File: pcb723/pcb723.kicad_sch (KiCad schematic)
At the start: 58 parts, among them J1 Conn_01x02_Pin, J2 Conn_01x02_Pin, J3 Conn_02x07_Odd_Even, J4 Conn_02x04_Odd_Even, J5 USB_C_Receptacle_USB2.0_16P, J6 Conn_02x13_Odd_Even, SW1 SW_Push, U1 STM32H723ZGT6, U2 AMS1117-3.3, Y1 8MHz 20pF

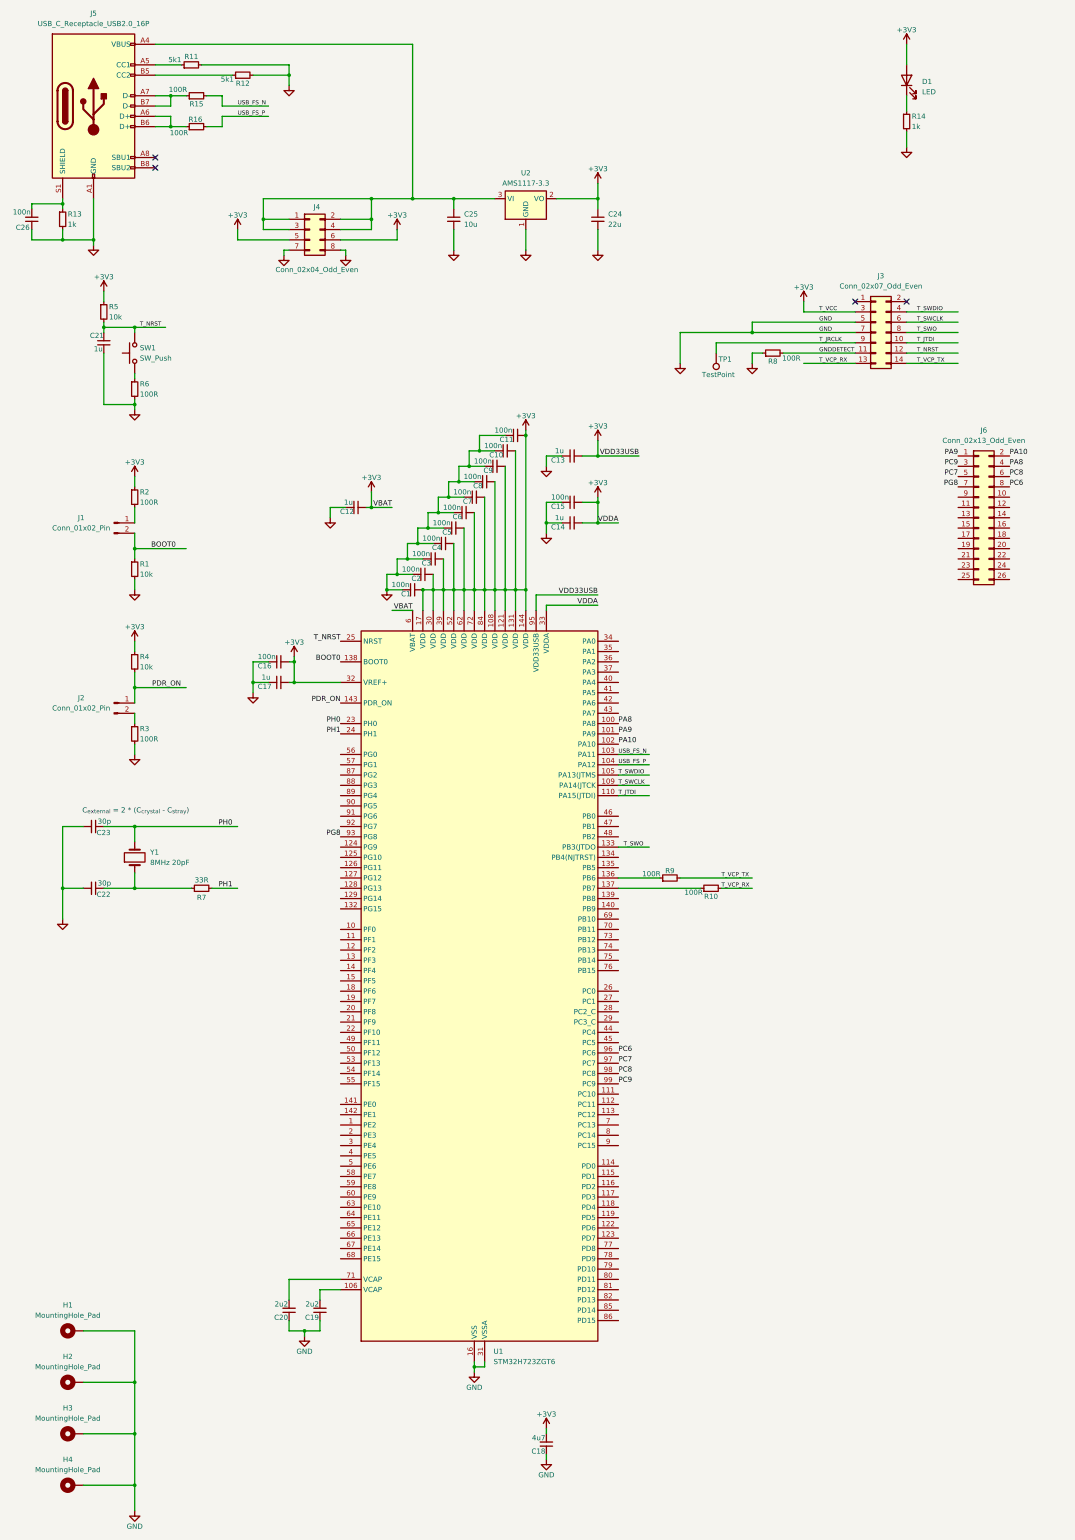
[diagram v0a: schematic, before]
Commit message: Connect starting breakout pins
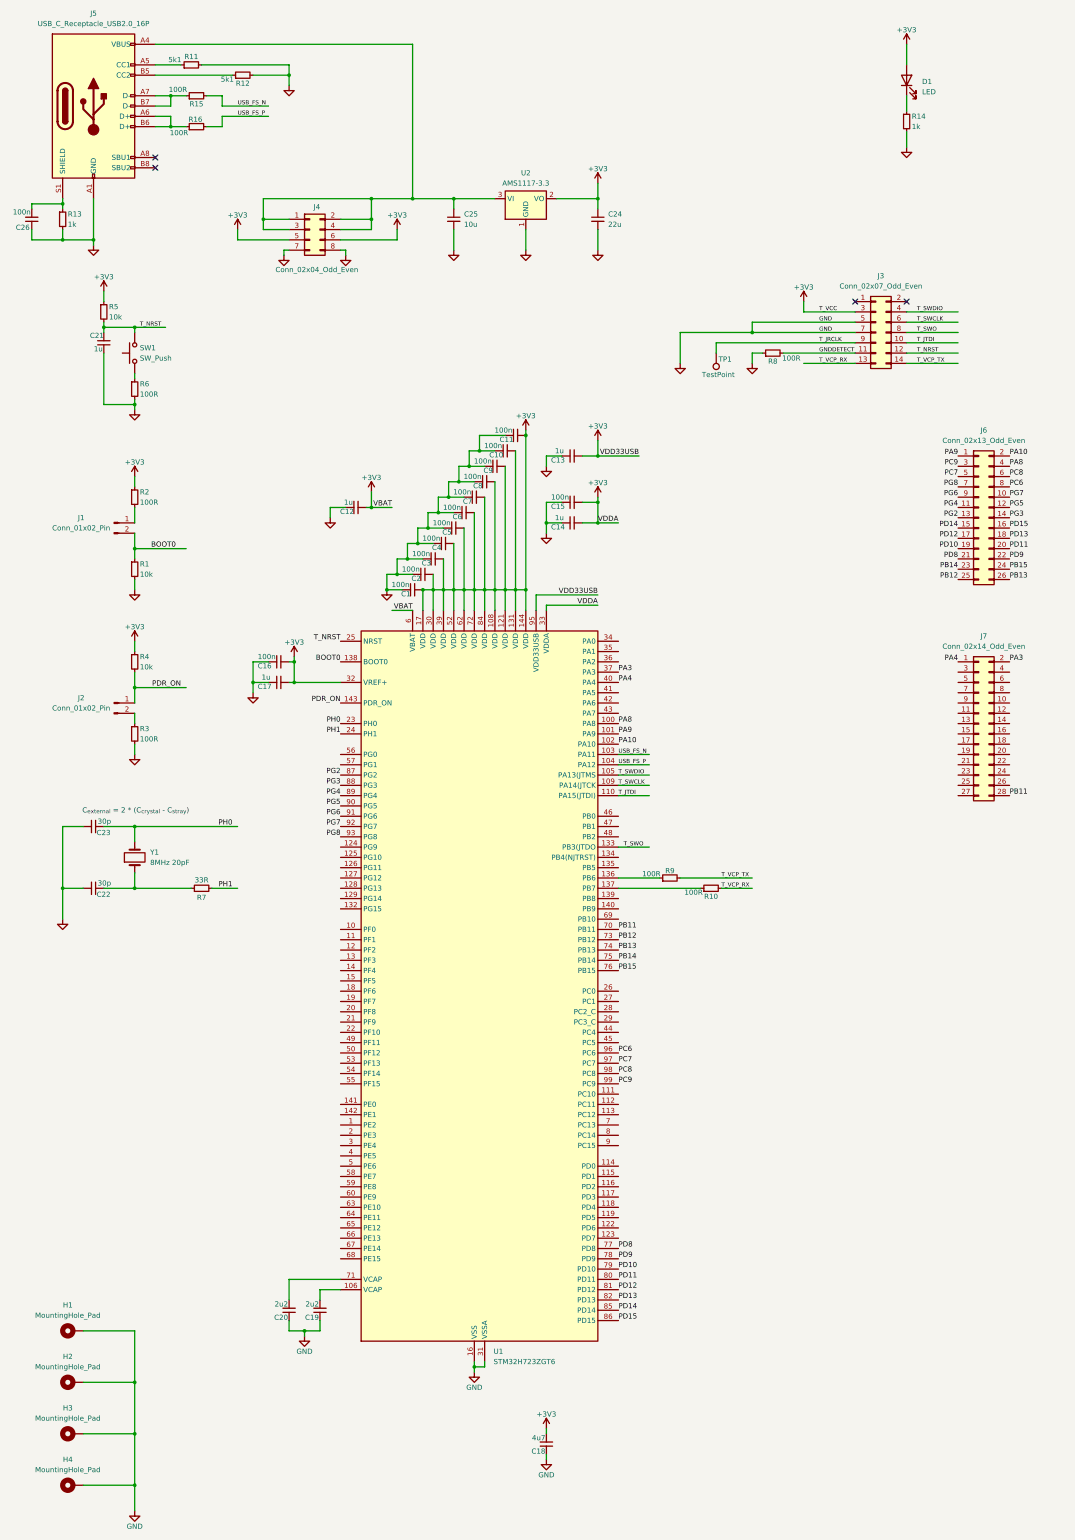
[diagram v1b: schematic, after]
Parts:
- added J7: Conn_02x14_Odd_Even, Connector_PinSocket_2.54mm:PinSocket_2x14_P2.54mm_Vertical, symbol Connector_Generic:Conn_02x14_Odd_Even
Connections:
- net PG7: now reaches J6.10 (Pin_10)
- net PG7: now also U1.92 (PG7)
- net PG4: now reaches J6.11 (Pin_11)
- net PG4: now also U1.89 (PG4)
- net PG5: now reaches J6.12 (Pin_12)
- net PG5: now also U1.90 (PG5)
- net PG2: now reaches J6.13 (Pin_13)
- net PG2: now also U1.87 (PG2)
- net PG3: now reaches J6.14 (Pin_14)
- net PG3: now also U1.88 (PG3)
- net PD14: now reaches J6.15 (Pin_15)
- net PD14: now also U1.85 (PD14)
- net PD15: now reaches J6.16 (Pin_16)
- net PD15: now also U1.86 (PD15)
- net PD12: now reaches J6.17 (Pin_17)
- net PD12: now also U1.81 (PD12)
- net PD13: now reaches J6.18 (Pin_18)
- net PD13: now also U1.82 (PD13)
- net PD10: now reaches J6.19 (Pin_19)
- net PD10: now also U1.79 (PD10)
- net PD11: now reaches J6.20 (Pin_20)
- net PD11: now also U1.80 (PD11)
- net PD8: now reaches J6.21 (Pin_21)
- net PD8: now also U1.77 (PD8)
- net PD9: now reaches J6.22 (Pin_22)
- net PD9: now also U1.78 (PD9)
- net PB14: now reaches J6.23 (Pin_23)
- net PB14: now also U1.75 (PB14)
- net PB15: now reaches J6.24 (Pin_24)
- net PB15: now also U1.76 (PB15)
- net PB12: now reaches J6.25 (Pin_25)
- net PB12: now also U1.73 (PB12)
- net PB13: now reaches J6.26 (Pin_26)
- net PB13: now also U1.74 (PB13)
- net PG6: now reaches J6.9 (Pin_9)
- net PG6: now also U1.91 (PG6)
- net PA3: now reaches U1.37 (PA3)
- net PA3: now also J7.2 (Pin_2)
- net PA4: now reaches U1.40 (PA4)
- net PA4: now also J7.1 (Pin_1)
- net PB11: now reaches U1.70 (PB11)
- net PB11: now also J7.28 (Pin_28)

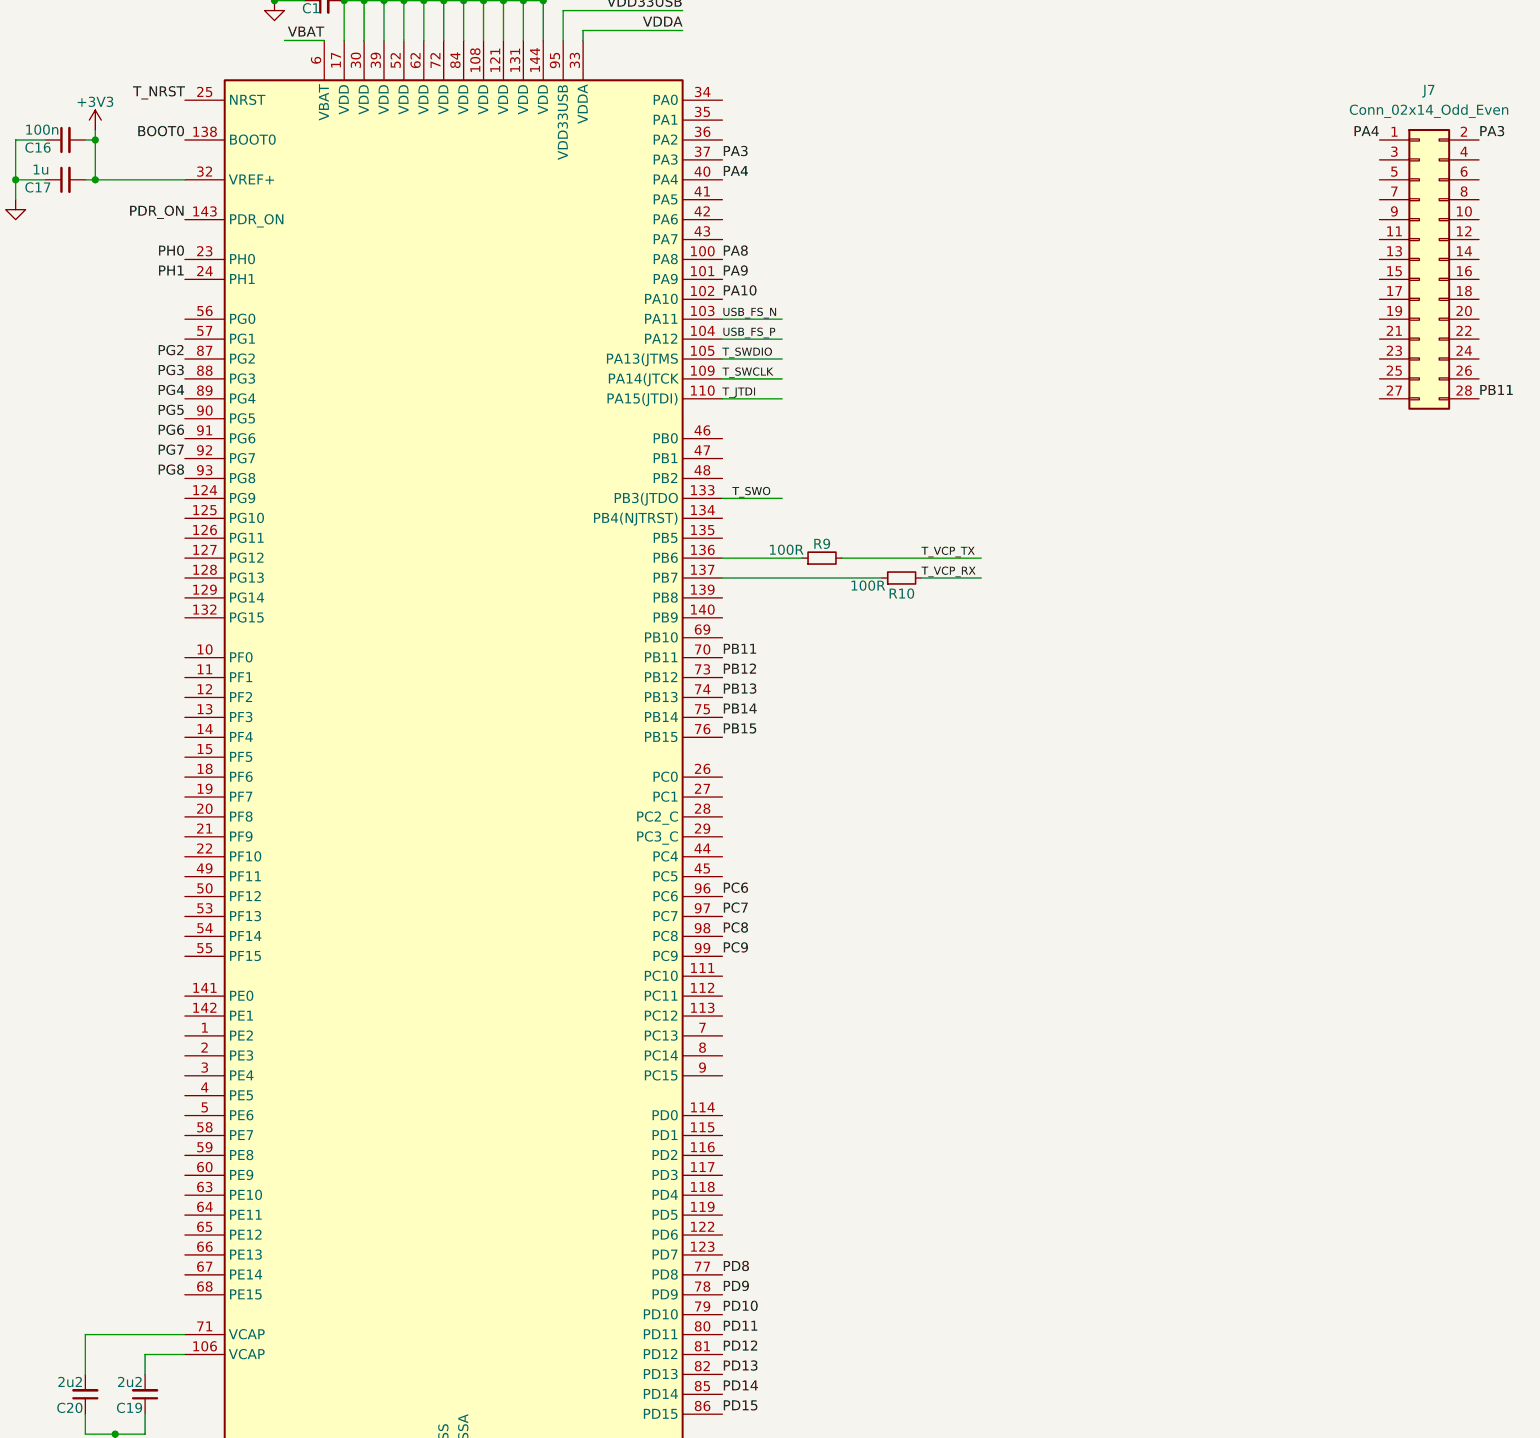
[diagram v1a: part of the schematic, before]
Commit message: Connect 28-pin socket header
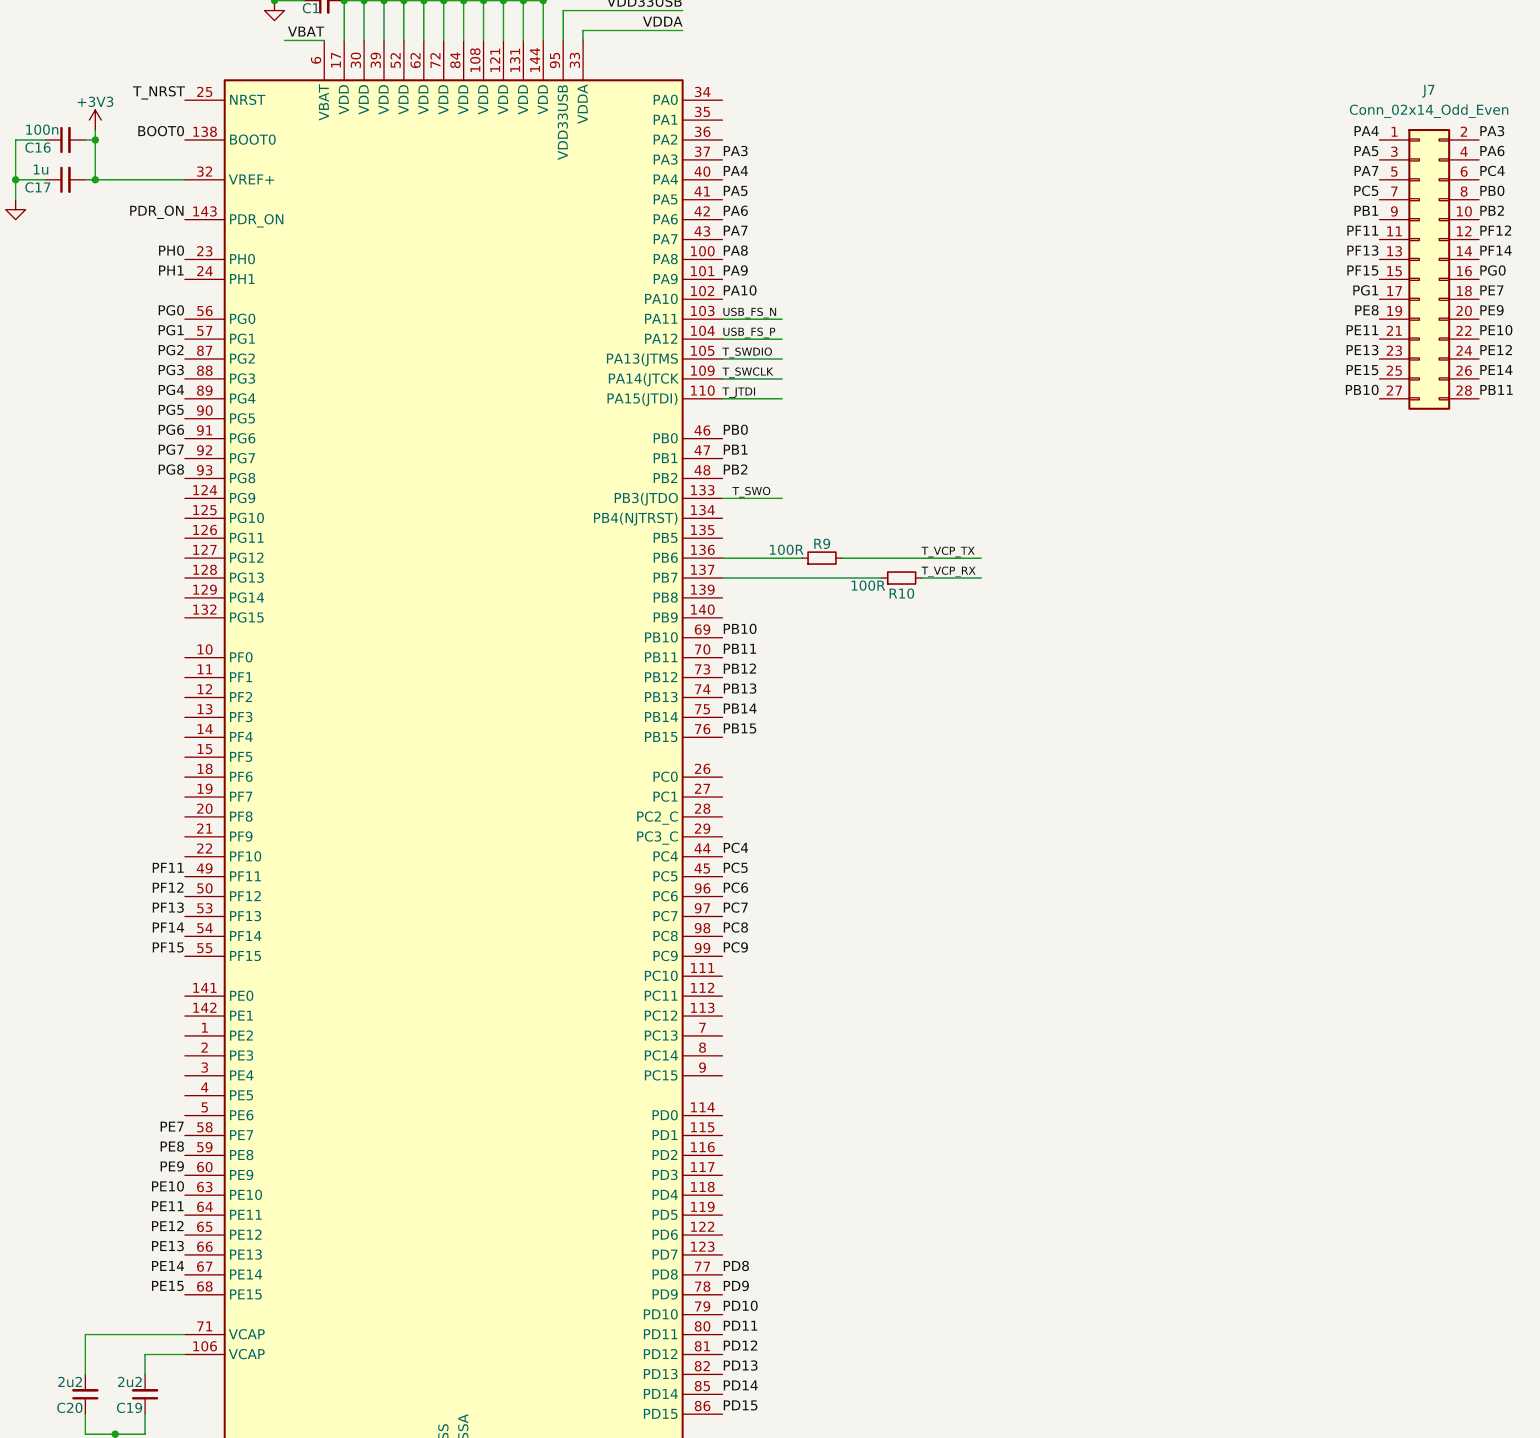
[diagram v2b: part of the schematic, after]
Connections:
- net PA5: now reaches U1.41 (PA5)
- net PA5: now also J7.3 (Pin_3)
- net PA6: now reaches U1.42 (PA6)
- net PA6: now also J7.4 (Pin_4)
- net PA7: now reaches U1.43 (PA7)
- net PA7: now also J7.5 (Pin_5)
- net PC4: now reaches U1.44 (PC4)
- net PC4: now also J7.6 (Pin_6)
- net PC5: now reaches U1.45 (PC5)
- net PC5: now also J7.7 (Pin_7)
- net PB0: now reaches U1.46 (PB0)
- net PB0: now also J7.8 (Pin_8)
- net PB1: now reaches U1.47 (PB1)
- net PB1: now also J7.9 (Pin_9)
- net PB2: now reaches U1.48 (PB2)
- net PB2: now also J7.10 (Pin_10)
- net PF11: now reaches U1.49 (PF11)
- net PF11: now also J7.11 (Pin_11)
- net PF12: now reaches U1.50 (PF12)
- net PF12: now also J7.12 (Pin_12)
- net PF13: now reaches U1.53 (PF13)
- net PF13: now also J7.13 (Pin_13)
- net PF14: now reaches U1.54 (PF14)
- net PF14: now also J7.14 (Pin_14)
- net PF15: now reaches U1.55 (PF15)
- net PF15: now also J7.15 (Pin_15)
- net PG0: now reaches U1.56 (PG0)
- net PG0: now also J7.16 (Pin_16)
- net PG1: now reaches U1.57 (PG1)
- net PG1: now also J7.17 (Pin_17)
- net PE7: now reaches U1.58 (PE7)
- net PE7: now also J7.18 (Pin_18)
- net PE8: now reaches U1.59 (PE8)
- net PE8: now also J7.19 (Pin_19)
- net PE9: now reaches U1.60 (PE9)
- net PE9: now also J7.20 (Pin_20)
- net PE10: now reaches U1.63 (PE10)
- net PE10: now also J7.22 (Pin_22)
- net PE11: now reaches U1.64 (PE11)
- net PE11: now also J7.21 (Pin_21)
- net PE12: now reaches U1.65 (PE12)
- net PE12: now also J7.24 (Pin_24)
- net PE13: now reaches U1.66 (PE13)
- net PE13: now also J7.23 (Pin_23)
- net PE14: now reaches U1.67 (PE14)
- net PE14: now also J7.26 (Pin_26)
- net PE15: now reaches U1.68 (PE15)
- net PE15: now also J7.25 (Pin_25)
- net PB10: now reaches U1.69 (PB10)
- net PB10: now also J7.27 (Pin_27)
